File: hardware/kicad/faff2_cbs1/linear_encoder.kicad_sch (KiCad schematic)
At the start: 22 parts, among them J601 FH12-10S-0.5SH(55), J602 FTSH-105-01-L-DV-K-TR, U601 AM26LV32

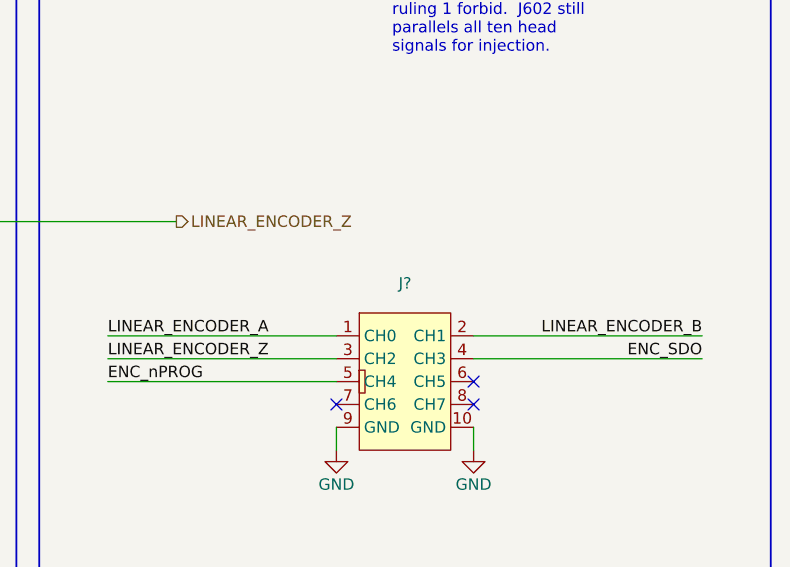
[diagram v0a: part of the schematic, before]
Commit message: review r5: the five verification findings, on top of the captain's state
Minimal deltas riding on his placement - nothing he moved is moved back unless
the finding was the move itself.

1. J603 and J1003 had lost their reference designators and both read "J?",
which merged them into a single netlist component: 17 nodes, pin numbers 3, 4,
5 and 10 twice, and only the 8510-4500PL's value and footprint, so the SAMTEC
SWD header had dropped out of the BOM altogether. Both references are set back
by hand, not by a blind re-annotate that would renumber other parts - and both
places that carry the name, the Reference property and the instance path's
(reference ...), because a sheet with those two disagreeing loads without
complaint and exports the old one. Proof: two distinct components now, J603
with 10 nodes on Amodo:8510-4500PL_LOGIC_TEST and J1003 with 14 on
Amodo:SAMTEC_SHF-107-01-L-D-SM, and the netlist export no longer warns about
annotation.

2. The +6V0 rename, completed again. c9d85d6 branched from 624bd13, one commit
before the rename, so the merge kept +6V0 on the net label, TP302's silkscreen
and the netlist net while restoring +5V5 in the title-block comment and four
note lines - leaving one note reading "+6V0 LMR33630 buck" two lines above "LDO
from +5V5". Those five, plus AGENTS.md, TEST_PLAN.md and
actuator-sch-power.md's current-state references, are back to +6V0. The
decisions-log history stays: DEC-P1 still explains why 5.5 V was chosen against
the TPS7A20's input maximum.

3. temp_sense: the ADS1120 block border sat at x=163.83, straight through
U701's body. The box is titled ADS1120 SUPPLIES AND SPI2 and U701 IS the
ADS1120, so the border goes to 151.13 - just left of the part, which is what
dragging it leftwards was reaching for - rather than back to 177.80.

4. power_rails: the two V24_LOGIC labels moved 1.27 mm left in the hand edit and
crossed the block border. The border moves instead, 13.97 -> 12.70, so his label
placement stands; 12.70 is the i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
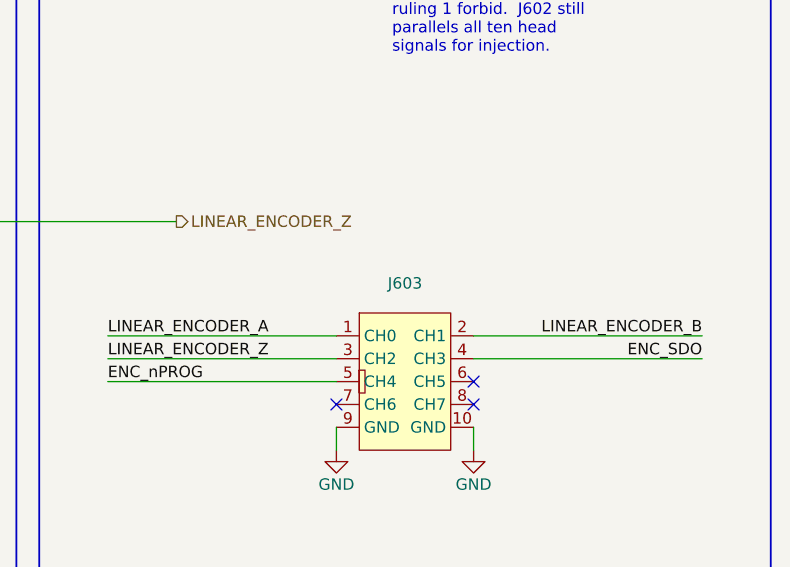
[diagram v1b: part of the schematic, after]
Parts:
- gave numbers to parts that had none: 1
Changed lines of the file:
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@@
 		(on_board yes)
 		(dnp no)
-		(property "Reference" "J?"
+		(property "Reference" "J603"
 			(at 220.98 97.03 0)
 			(effects
@@
 			(project "faff2_cbs1"
 				(path "/5edb00fd-45c9-5fe7-8d71-adbf38f38546/7f1522a2-4954-524c-ba63-158dc350920f"
-					(reference "J?")
+					(reference "J603")
 					(unit 1)
 				)
